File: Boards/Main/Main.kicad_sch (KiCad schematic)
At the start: 25 parts, among them J1 Power, J2 PWM 7-0, J3 Digital, J5 Conn_01x16, J6 Conn_01x16, Q1 16 MHz, SW1 RESET, U3 WD42C22, U4 6116 SRAM

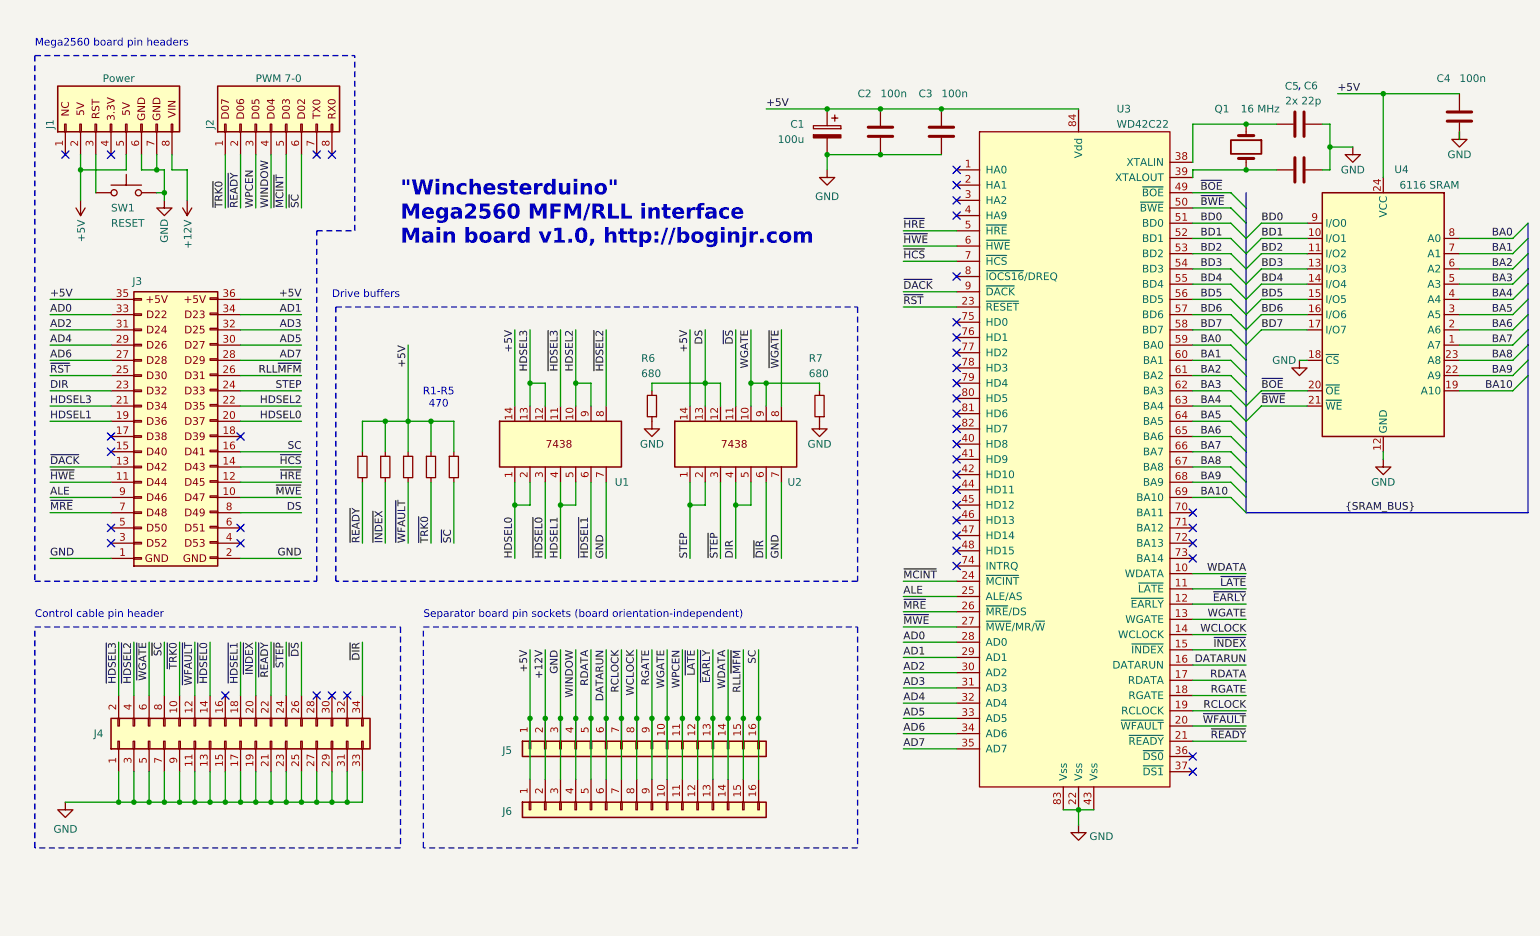
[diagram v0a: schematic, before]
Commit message: v1.1 mainboard: add microSD card support, 32K buffer SRAM
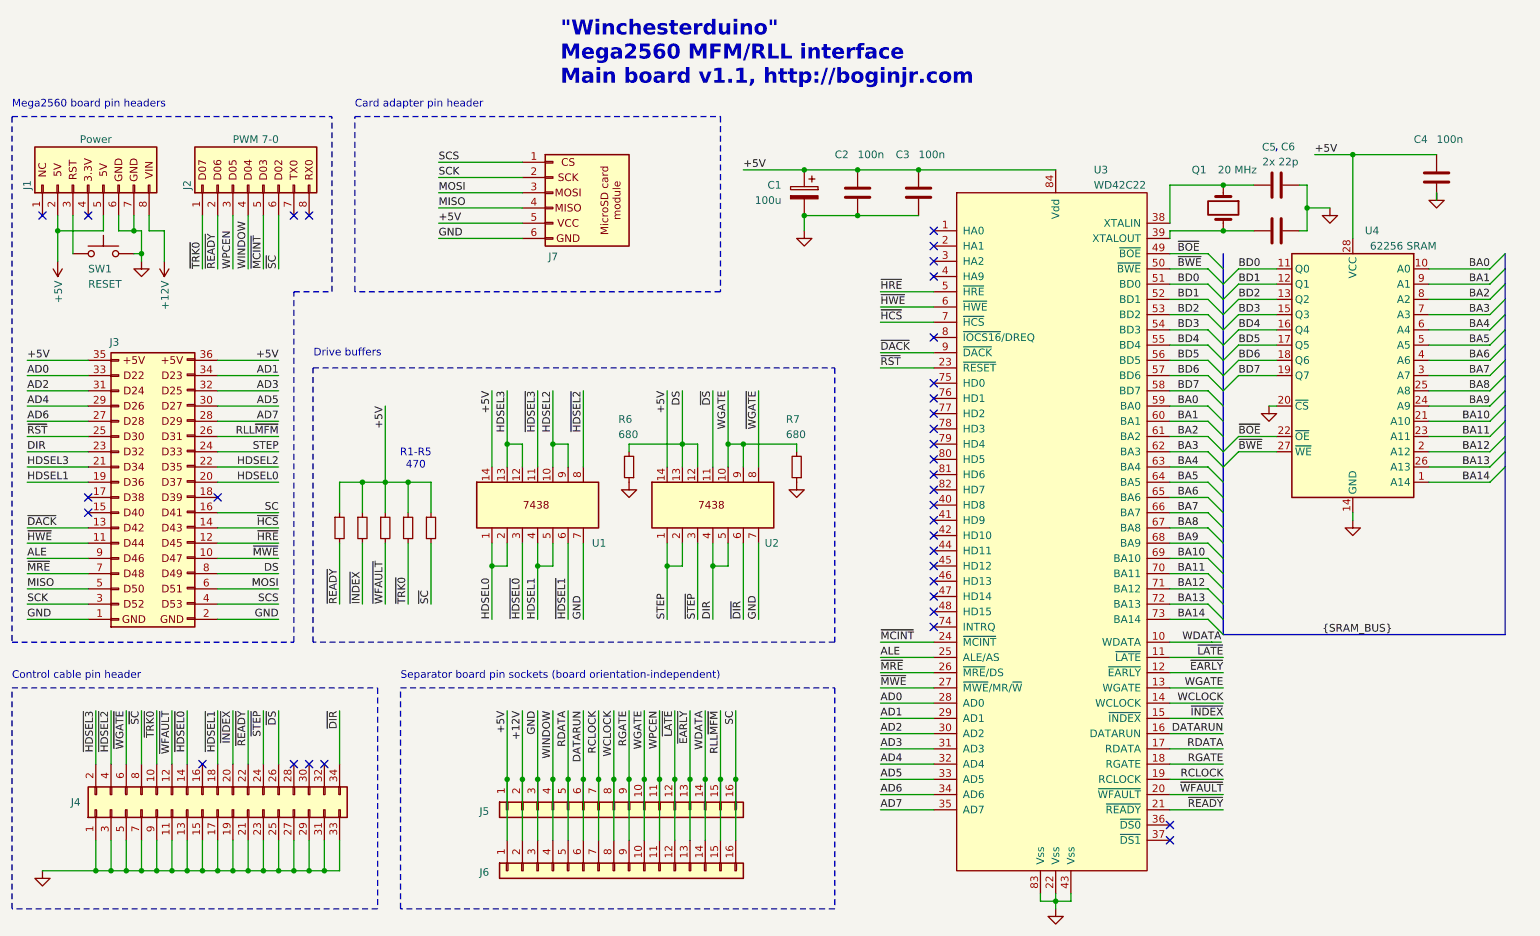
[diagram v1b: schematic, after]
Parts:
- removed U4: 6116 SRAM, Package_DIP:DIP-24_W15.24mm_LongPads, symbol Memory_RAM:HY6264AxP
- added J7: Digital, Connector_PinHeader_2.54mm:PinHeader_1x06_P2.54mm_Vertical, symbol Connector_Generic:Conn_02x18_Odd_Even
- added U4: 62256 SRAM, Package_DIP:DIP-28_W15.24mm_LongPads, symbol Memory_RAM:CY62256-70PC
- Q1: value 16 MHz -> 20 MHz
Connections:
- net +5V: now also J7.5 (Pin_5), U4.28 (VCC)
- net BA0: now also U4.10 (A0)
- net BA1: now also U4.9 (A1)
- net BA10: now also U4.21 (A10)
- net BA2: now also U4.8 (A2)
- net BA3: now also U4.7 (A3)
- net BA4: now also U4.6 (A4)
- net BA5: now also U4.5 (A5)
- net BA6: now also U4.4 (A6)
- net BA7: now also U4.3 (A7)
- net BA8: now also U4.25 (A8)
- net BA9: now also U4.24 (A9)
- net BD0: now also U4.11 (Q0)
- net BD1: now also U4.12 (Q1)
- net BD2: now also U4.13 (Q2)
- net BD3: now also U4.15 (Q3)
- net BD4: now also U4.16 (Q4)
- net BD5: now also U4.17 (Q5)
- net BD6: now also U4.18 (Q6)
- net BD7: now also U4.19 (Q7)
- net GND: now also J7.6 (Pin_6), U4.14 (GND), U4.20 (~{CS})
- net ~{BOE}: now also U4.22 (~{OE})
- net ~{BWE}: now also U4.27 (~{WE})
- net SCK: now reaches J3.3 (Pin_3)
- net SCK: now also J7.2 (Pin_2)
- net SCS: now reaches J3.4 (Pin_4)
- net SCS: now also J7.1 (Pin_1)
- net MISO: now reaches J3.5 (Pin_5)
- net MISO: now also J7.4 (Pin_4)
- net MOSI: now reaches J3.6 (Pin_6)
- net MOSI: now also J7.3 (Pin_3)
- net BA11: now reaches U3.70 (BA11)
- net BA11: now also U4.23 (A11)
- net BA12: now reaches U3.71 (BA12)
- net BA12: now also U4.2 (A12)
- net BA13: now reaches U3.72 (BA13)
- net BA13: now also U4.26 (A13)
- net BA14: now reaches U3.73 (BA14)
- net BA14: now also U4.1 (A14)
- no-connect marks 43 -> 35
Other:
- note added: ""Winchesterduino" Mega2560 MFM/RLL interface Main board v1.1, http://boginjr.com"
- note added: "Card adapter pin header"
- note removed: ""Winchesterduino" Mega2560 MFM/RLL interface Main board v1.0, http://boginjr.com"
- moved on the sheet: C1, C2, C3, C4, C5, C6, J1, J2, J3, J4, J5, J6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

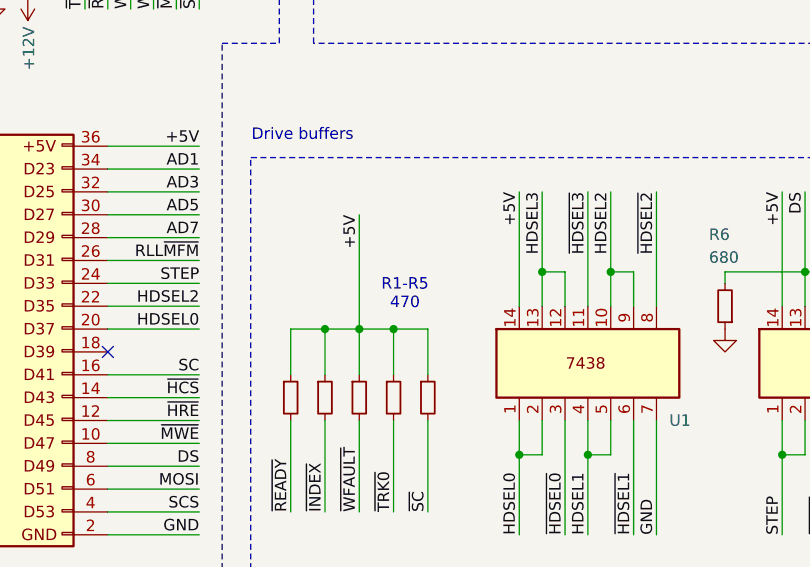
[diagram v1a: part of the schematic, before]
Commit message: Fix typo in schematic; add SD file buffer flush
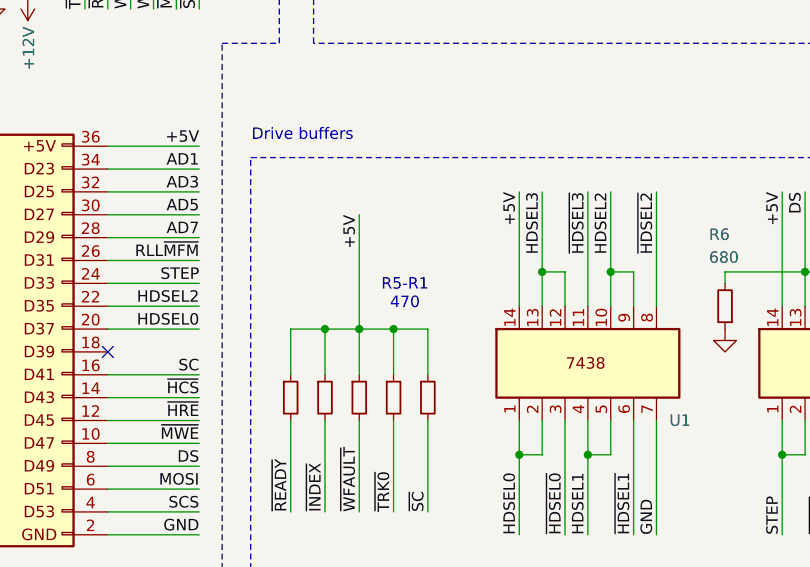
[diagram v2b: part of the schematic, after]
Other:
- note added: "R5-R1 470"
- note removed: "R1-R5 470"
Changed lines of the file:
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@@
 		)
 	)
-	(text "R1-R5\n470"
+	(text "R5-R1\n470"
 		(exclude_from_sim no)
 		(at 90.17 101.6 0)
